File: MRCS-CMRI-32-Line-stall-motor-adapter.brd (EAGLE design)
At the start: 106 x 100 mm, 4 parts

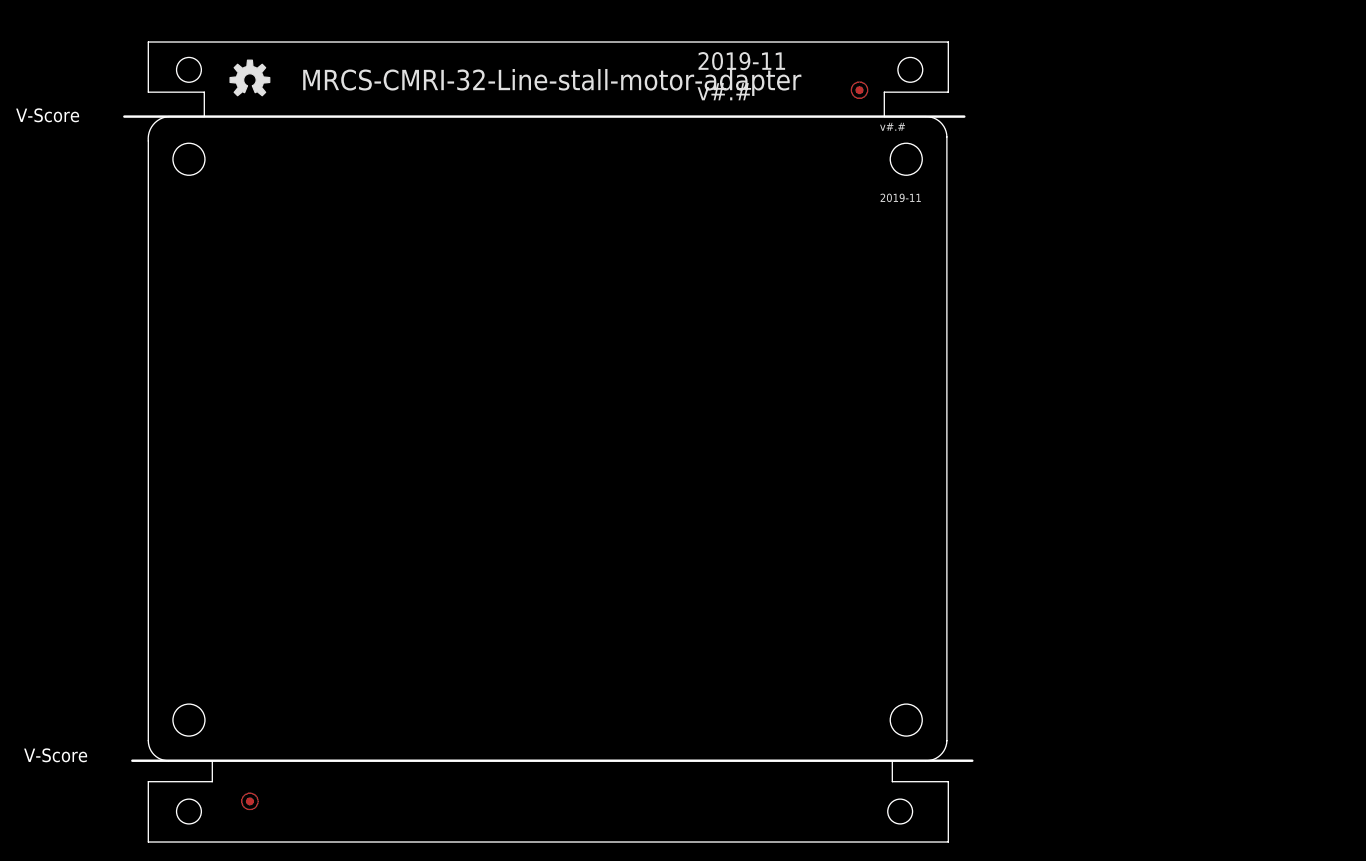
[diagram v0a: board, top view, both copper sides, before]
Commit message: clean up at end of Version 1.0
made pdfs of Schematic and layout, cleaned up work files.  This version passes all electrical design rules and created a believable set of gerbers
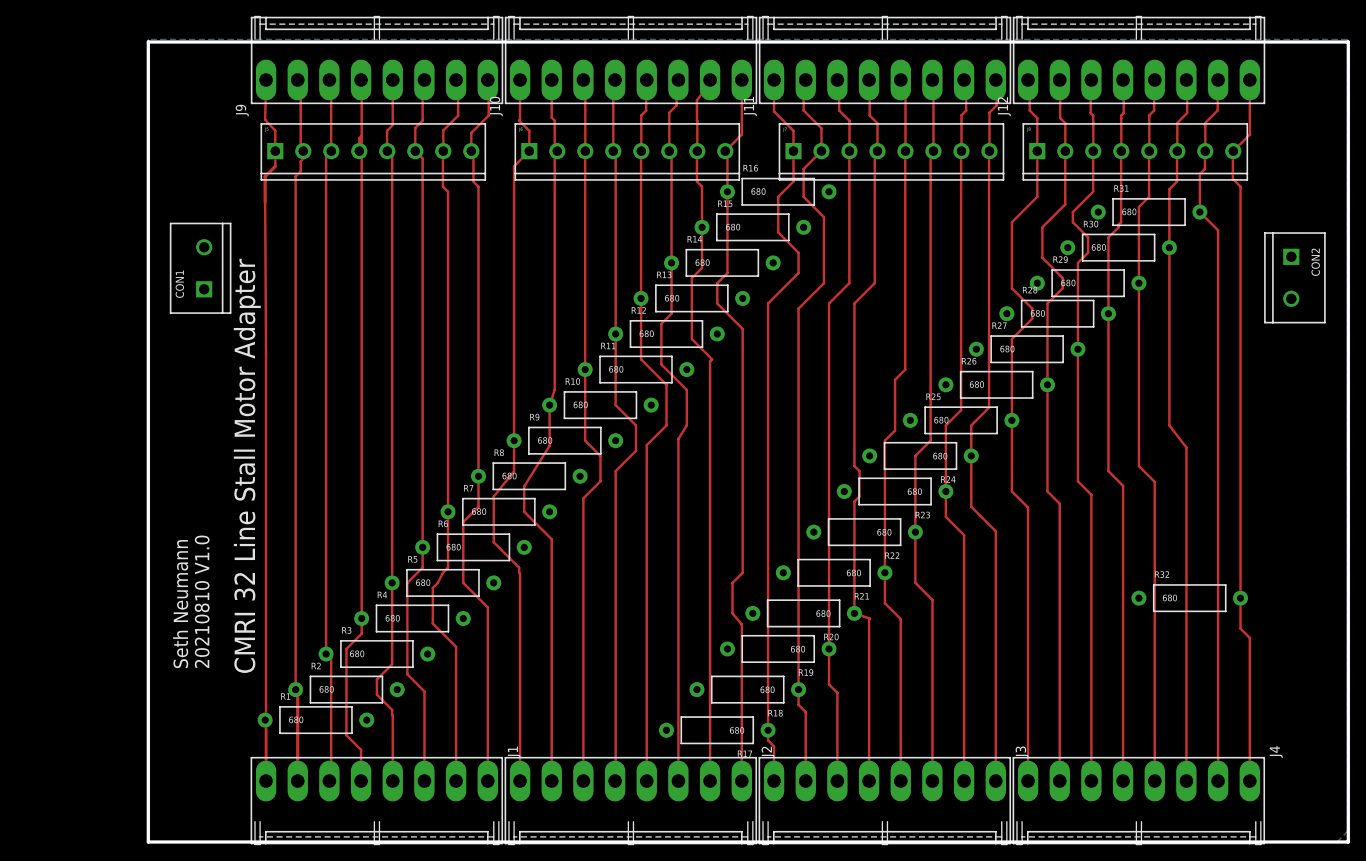
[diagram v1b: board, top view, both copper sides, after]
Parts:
- removed BOARD1: BOARD80X100, SPCoast:BOARD-DINRAIL-3.17INX10CM
- removed FID1, FID2: FIDUCIAL, SPCoast:FIDUCIAL_1MM
- removed OSHW1: DOC-OSHW-LOGO-M, SPCoast:OSHW-LOGO-M
- added CON1: 12V in, SPCoast:SCREWTERMINAL-5MM-2
- added CON2: 12V Out, SPCoast:SCREWTERMINAL-5MM-2
- added J1: Input A, SPCoast:KK-156-8-F
- added J10: Output B (M), SPCoast:KK-156-8-F
- added J11: Output C (M), SPCoast:KK-156-8-F
- added J12: Output D (M), SPCoast:KK-156-8-F
- added J2: Input B, SPCoast:KK-156-8-F
- added J3: Input C, SPCoast:KK-156-8-F
- added J4: Input D, SPCoast:KK-156-8-F
- added J5: Output A (35), SPCoast:SCREWTERMINAL-3.5MM-8
- added J6: Output B (35), SPCoast:SCREWTERMINAL-3.5MM-8
- added J7: OutputC (35), SPCoast:SCREWTERMINAL-3.5MM-8
- added J8: Output D (35), SPCoast:SCREWTERMINAL-3.5MM-8
- added J9: Output A (M), SPCoast:KK-156-8-F
- added R1, R10, R11, R12, R13, R14, R15, R16, R17, R18, R19, R2, R20, R21, R22, R23, R24, R25, R26, R27, R28, R29, R3, R30, R31, R32, R4, R5, R6, R7, R8, R9: 680, SparkFun-Passives:AXIAL-0.5
- added U$1: (no value), MRCSLogoTop:MRCSLOGOTOP
- added U$2: (no value), MRCSLogoBtm:MRCSLOGOBTM
- added U$3: (no value), MRCS-prop65warningBtm:CA-PROP65WARNING
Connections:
- new net +12V: CON1.1, CON1.2, CON2.1, CON2.2, R1.P$2, R10.P$2, R11.P$2, R12.P$2, R13.P$2, R14.P$2, R15.P$2, R16.P$2, R17.P$2, R18.P$2, R19.P$2, R2.P$2, R20.P$2, R21.P$2, R22.P$2, R23.P$2, R24.P$2, R25.P$1, R26.P$1, R27.P$1, R28.P$1, R29.P$1, R3.P$2, R30.P$1, R31.P$1, R32.P$1, R4.P$2, R5.P$2, R6.P$2, R7.P$2, R8.P$2, R9.P$2
- new net N$1: J1.5, J5.4, J9.4, R4.P$1
- new net N$10: J1.3, J5.6, J9.6, R6.P$1
- new net N$11: J1.2, J5.7, J9.7, R7.P$1
- new net N$12: J1.1, J5.8, J9.8, R8.P$1
- new net N$13: J1.6, J5.3, J9.3, R3.P$1
- new net N$14: J10.2, J2.7, J6.2, R10.P$1
- new net N$15: J10.7, J2.2, J6.7, R15.P$1
- new net N$16: J10.8, J2.1, J6.8, R16.P$1
- new net N$17: J10.4, J2.5, J6.4, R12.P$1
- new net N$18: J11.2, J3.7, J7.2, R18.P$1
- new net N$19: J11.3, J3.6, J7.3, R19.P$1
- new net N$2: J1.8, J5.1, J9.1, R1.P$1
- new net N$20: J11.4, J3.5, J7.4, R20.P$1
- new net N$21: J11.5, J3.4, J7.5, R21.P$1
- new net N$22: J11.6, J3.3, J7.6, R22.P$1
- new net N$23: J11.7, J3.2, J7.7, R23.P$1
- new net N$24: J11.8, J3.1, J7.8, R24.P$1
- new net N$25: J12.1, J4.8, J8.1, R25.P$2
- new net N$26: J12.2, J4.7, J8.2, R26.P$2
- new net N$27: J12.3, J4.6, J8.3, R27.P$2
- new net N$28: J12.4, J4.5, J8.4, R28.P$2
- new net N$29: J12.5, J4.4, J8.5, R29.P$2
- new net N$3: J10.1, J2.8, J6.1, R9.P$1
- new net N$30: J12.6, J4.3, J8.6, R30.P$2
- new net N$31: J12.7, J4.2, J8.7, R31.P$2
- new net N$32: J12.8, J4.1, J8.8, R32.P$2
- new net N$4: J1.7, J5.2, J9.2, R2.P$1
- new net N$5: J10.3, J2.6, J6.3, R11.P$1
- new net N$6: J11.1, J3.8, J7.1, R17.P$1
- new net N$7: J10.5, J2.4, J6.5, R13.P$1
- new net N$8: J10.6, J2.3, J6.6, R14.P$1
- new net N$9: J1.4, J5.5, J9.5, R5.P$1
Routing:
- net N$2: track 0.00 -> 96.3 mm
- net N$6: track 0.00 -> 92.4 mm
- net N$25: track 0.00 -> 92.4 mm
- net N$18: track 0.00 -> 92.3 mm
- net N$1: track 0.00 -> 91.9 mm
- net N$26: track 0.00 -> 91.6 mm
- net N$16: track 0.00 -> 91.4 mm
- net N$20: track 0.00 -> 91.3 mm
- net N$3: track 0.00 -> 91.2 mm
- net N$12: track 0.00 -> 91.0 mm
- net N$27: track 0.00 -> 90.9 mm
- net N$11: track 0.00 -> 90.7 mm
- net N$14: track 0.00 -> 90.5 mm
- net N$8: track 0.00 -> 90.4 mm
- net N$7: track 0.00 -> 90.3 mm
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- added copper zone on layer 16, net +12V
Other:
- board size 106 x 100 mm -> 150 x 100 mm
- board text added: "CMRI 32 Line Stall Motor Adapter"
- board text added: "Seth Neumann 20210810 V1.0"
- board text removed: "2019-11"
- board text removed: ">DRAWING_NAME"
- board text removed: "v#.#"
